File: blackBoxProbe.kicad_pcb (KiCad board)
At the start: 4 copper layers, 44 x 44 mm, 77 parts, among them J1 USB-ID, J2 JTAG_2X05, J3 JTAG_2X05, J4 Conn_01x04, Q1 Q_NMOS_DUAL, Q2 Q_PMOS_DUAL, U1 MCP1702-MB, U2 USBLC6-2, U3 STM32F103CBT, U4 74X2T45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

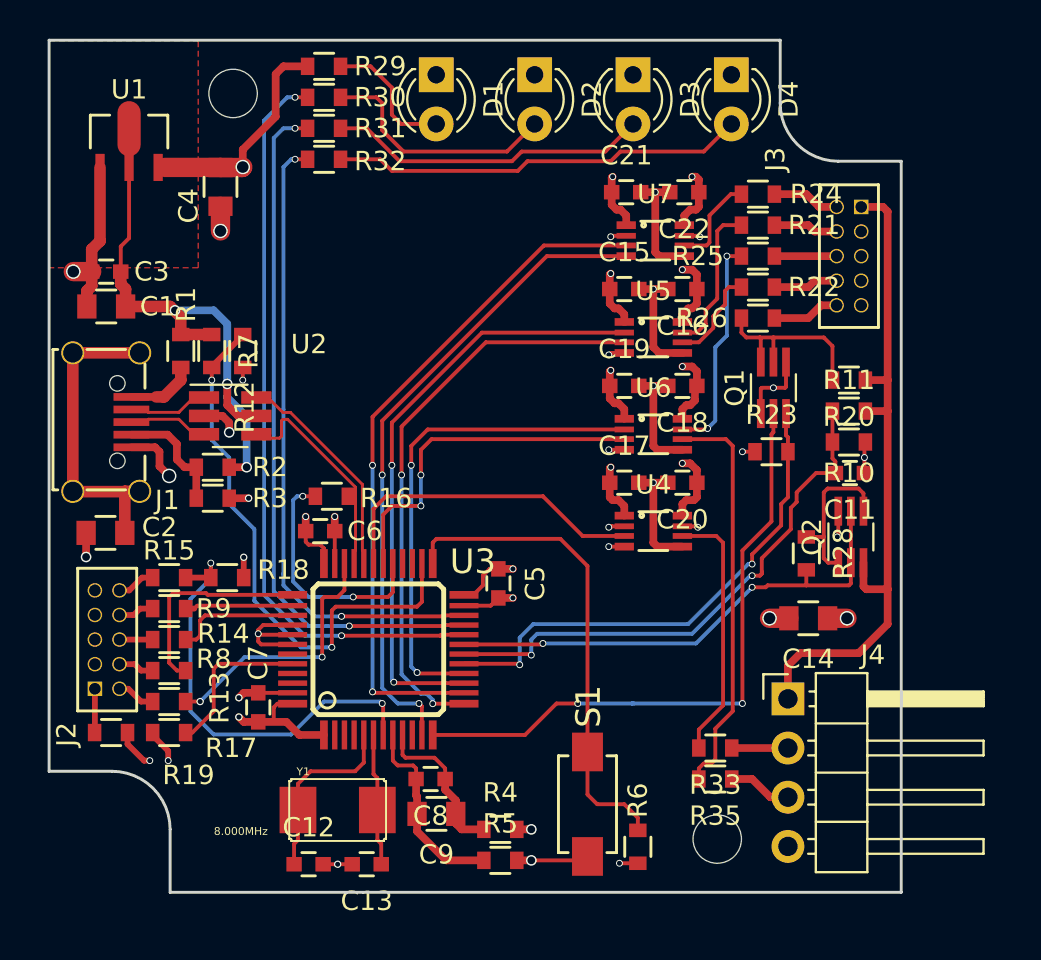
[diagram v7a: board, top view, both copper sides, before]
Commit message: FIX: forgotten one disconnected net
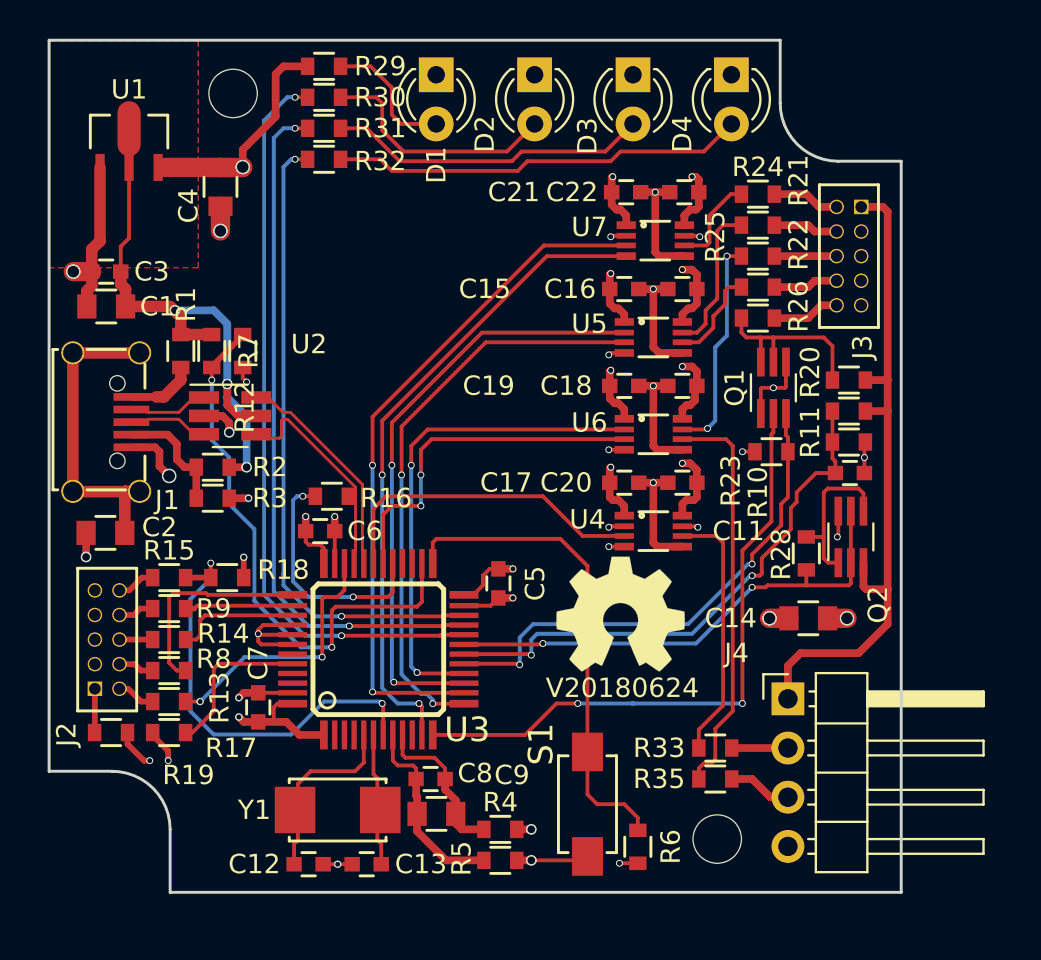
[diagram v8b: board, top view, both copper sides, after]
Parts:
- C12, C13: value C -> 10p
- N1: moved to F.Cu
- N2: value V20180330 -> V20180624
- Y1: footprint SquantorCrystal:SquantorCrystal-CRYSTAL_5.0X3.2 -> SquantorCrystal:X_5.0_3.2
- moved N1 19.1 mm to (43.8, 180.9), turned to 0 degrees
